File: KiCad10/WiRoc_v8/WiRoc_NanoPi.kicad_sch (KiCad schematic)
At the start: 51 parts, among them J10 Conn_01x09_Socket, J12 TC2050, J2 Conn_01x04, J5 Conn_01x04_Socket, J6 HAT_Conn_DBG, J8 Conn_01x06, SW1 SW_SPST, U1 SY6280, U10 SY7069ADC, U2 OLED, U3 AXP209, U5 SY6280, U6 BatteryPadM, U7 BatteryPadP

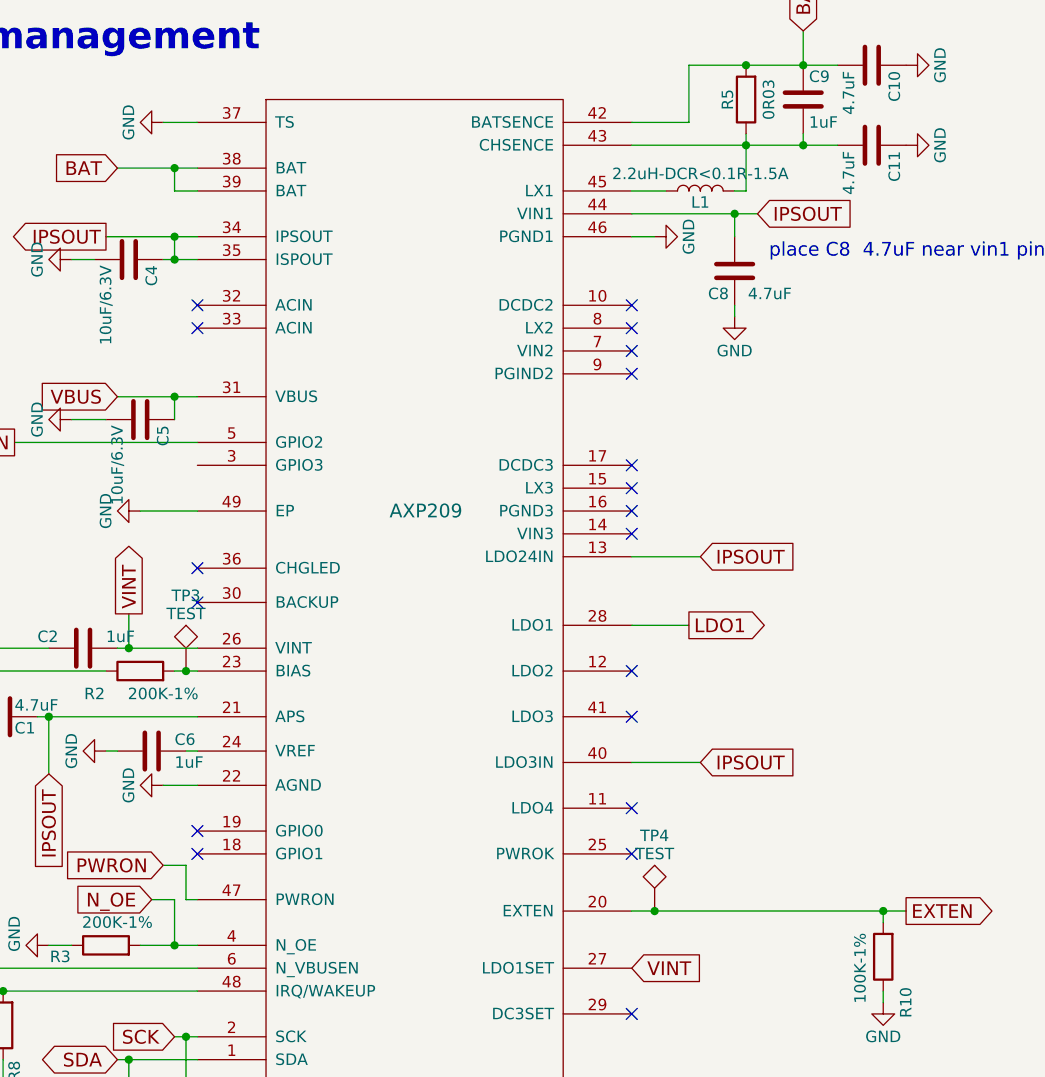
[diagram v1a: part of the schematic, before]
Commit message: add logo, improve layout
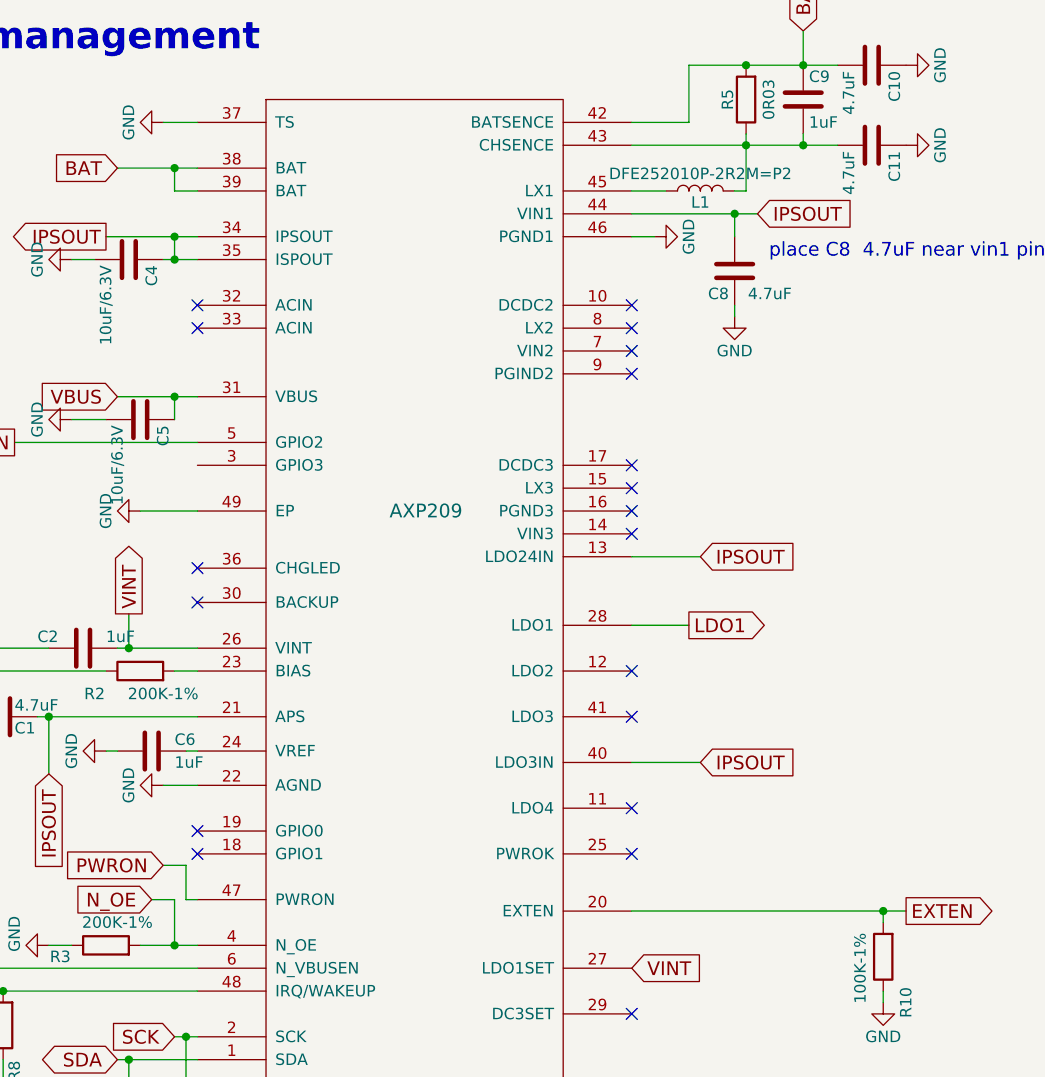
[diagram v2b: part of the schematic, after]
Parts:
- removed TP3, TP4: TEST, TestPoint:TestPoint_Pad_D1.0mm, symbol WiRoc:TEST
- L1: value 2.2uH-DCR<0.1R-1.5A -> DFE252010P-2R2M=P2; footprint WiRoc:Inductor_SLW4018 -> Inductor_SMD:L_1008_2520Metric; LCSC Part # C206341 -> C576403; Manufacturer Sunltech Tech -> Murata Electronics; ManufacturerPartNumber SLW4018S2R2MST -> DFE252012F‑2R2M=P2; Package 4018 -> 1008; WebsiteURL https://lcsc.com/product-detail/Power-Inductors_2-2uH-20-1-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 -> (none)
- L3: footprint WiRoc:Inductor_SLW4018 -> Inductor_SMD:L_1008_2520Metric; LCSC Part # C206395 -> C909806; Manufacturer Sunltech Tech -> Murata Electronics; ManufacturerPartNumber SLW4020S1R5MST -> DFE252012F-1R5M=P2

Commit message: etc
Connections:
- no-connect marks 26 -> 27
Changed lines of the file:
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@@
-	)
-	(junction
-		(at 43.18 20.32)
-		(diameter 0)
-		(color 0 0 0 0)
 	)
 	(junction
@@
 		(at 137.16 38.1)
 	)
+	(no_connect
+		(at 54.61 111.76)
+	)
 	(polyline
 		(pts
@@
 		)
 		(stroke
-			(width 0)
-			(type default)
-		)
-	)
-	(wire
-		(pts
-			(xy 41.91 20.32) (xy 43.18 20.32)
-		)
-		(stroke
